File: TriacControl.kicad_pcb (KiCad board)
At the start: 2 copper layers, 100 x 53 mm, 55 parts, among them J1 AC LINE, J2 LOAD, J3 ZEROCROSS, J4 PWM, Q1 BT136-600, Q2 2N3906, U1 MOC3020M, U2 PC817, U3 PC817

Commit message: A few changes
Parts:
- added R27: 2k2, Resistor_THT:R_Axial_DIN0207_L6.3mm_D2.5mm_P7.62mm_Horizontal, F.Cu at (98.5, 94.1)
- Q2: value 2N3906 -> 2N2907
- R23, R24: value 100R -> 10R
- R25: value 10k -> 220R
- R26: value 22k -> 2k2
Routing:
- net Net-(D1-A): track 29.1 -> 38.0 mm
- net Net-(D2-A): track 16.8 -> 20.4 mm
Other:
- board text added: "MOC3021"
- board text removed: "MOC3081"
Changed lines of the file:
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@@
   )
   (footprint "Resistor_THT:R_Axial_DIN0207_L6.3mm_D2.5mm_P7.62mm_Horizontal" (layer "F.Cu")
+    (at 98.47 94.08 180)
+    (descr "Resistor, Axial_DIN0207 series, Axial, Horizontal, pin pitch=7.62mm, 0.25W = 1/4W, length*diameter=6.3*2.5mm^2, http://cdn-reichelt.de/documents/datenblatt/B400/1_4W%23YAG.pdf")
+    (tags "Resistor Axial_DIN0207 series Axial Horizontal pin pitch 7.62mm 0.25W = 1/4W length 6.3mm diameter 2.5mm")
+    (property "Sheetfile" "TriacControl.kicad_sch")
+    (property "Sheetname" "")
+    (property "ki_description" "Resistor")
+    (property "ki_keywords" "R res resistor")
+    (attr through_hole)
+    (fp_text reference "R27" (at 3.74 0.06) (layer "F.SilkS")
+        (effects (font (size 1 1) (thickness 0.15)))
+    )
+    (fp_text value "2k2" (at 3.81 2.37) (layer "F.Fab")
+        (effects (font (size 1 1) (thickness 0.15)))
+    )
+    (fp_text user "${REFERENCE}" (at 3.81 0) (layer "F.Fab")
+        (effects (font (size 1 1) (thickness 0.15)))
+    )
+    (fp_line (start 0.54 -1.37) (end 7.08 -1.37)
+      (stroke (width 0.12) (type solid)) (layer "F.SilkS"))
+    (fp_line (start 0.54 -1.04) (end 0.54 -1.37)
+      (stroke (width 0.12) (type solid)) (layer "F.SilkS"))
+    (fp_line (start 0.54 1.04) (end 0.54 1.37)
+      (stroke (width 0.12) (type solid)) (layer "F.SilkS"))
+    (fp_line (start 0.54 1.37) (end 7.08 1.37)
+      (stroke (width 0.12) (type solid)) (layer "F.SilkS"))
+    (fp_line (start 7.08 -1.37) (end 7.08 -1.04)
+      (stroke (width 0.12) (type solid)) (layer "F.SilkS"))
+    (fp_line (start 7.08 1.37) (end 7.08 1.04)
+      (stroke (width 0.12) (type solid)) (layer "F.SilkS"))
+    (fp_line (start -1.05 -1.5) (end -1.05 1.5)
+      (stroke (width 0.05) (type solid)) (layer "F.CrtYd"))
+    (fp_line (start -1.05 1.5) (end 8.67 1.5)
+      (stroke (width 0.05) (type solid)) (layer "F.CrtYd"))
+    (fp_line (start 8.67 -1.5) (end -1.05 -1.5)
+      (stroke (width 0.05) (type solid)) (layer "F.CrtYd"))
+    (fp_line (start 8.67 1.5) (end 8.67 -1.5)
+      (stroke (width 0.05) (type solid)) (layer "F.CrtYd"))
+    (fp_line (start 0 0) (end 0.66 0)
+      (stroke (width 0.1) (type solid)) (layer "F.Fab"))
+    (fp_line (start 0.66 -1.25) (end 0.66 1.25)
+      (stroke (width 0.1) (type solid)) (layer "F.Fab"))
+    (fp_line (start 0.66 1.25) (end 6.96 1.25)
+      (stroke (width 0.1) (type solid)) (layer "F.Fab"))
+    (fp_line (start 6.96 -1.25) (end 0.66 -1.25)
+      (stroke (width 0.1) (type solid)) (layer "F.Fab"))
+    (fp_line (start 6.96 1.25) (end 6.96 -1.25)
+      (stroke (width 0.1) (type solid)) (layer "F.Fab"))
+    (fp_line (start 7.62 0) (end 6.96 0)
+      (stroke (width 0.1) (type solid)) (layer "F.Fab"))
+    (pad "1" thru_hole circle (at 0 0 180) (size 1.6 1.6) (drill 0.8) (layers "*.Cu" "*.Mask")
+      (net 8 "Net-(D1-A)") (pintype "passive"))
+    (pad "2" thru_hole oval (at 7.62 0 180) (size 1.6 1.6) (drill 0.8) (layers "*.Cu" "*.Mask")
+      (net 9 "Net-(D2-A)") (pintype "passive"))
+    (model "${KICAD6_3DMODEL_DIR}/Resistor_THT.3dshapes/R_Axial_DIN0207_L6.3mm_D2.5mm_P7.62mm_Horizontal.wrl"
+      (offset (xyz 0 0 0))
+      (scale (xyz 1 1 1))
+      (rotate (xyz 0 0 0))
+    )
+  )
+  (footprint "Resistor_THT:R_Axial_DIN0207_L6.3mm_D2.5mm_P7.62mm_Horizontal" (layer "F.Cu")
     (at 115.85 62.2 -90)
     (descr "Resistor, Axial_DIN0207 series, Axial, Horizontal, pin pitch=7.62mm, 0.25W = 1/4W, length*diameter=6.3*2.5mm^2, http://cdn-reichelt.de/documents/datenblatt/B400/1_4W%23YAG.pdf")
@@
         (effects (font (size 1 1) (thickness 0.15)))
     )
-    (fp_text value "100R" (at 3.81 2.37 90) (layer "F.Fab")
+    (fp_text value "10R" (at 3.81 2.37 90) (layer "F.Fab")
         (effects (font (size 1 1) (thickness 0.15)))
     )
@@
         (effects (font (size 1 1) (thickness 0.15)))
     )
-    (fp_text value "100R" (at 3.81 2.37 90) (layer "F.Fab")
+    (fp_text value "10R" (at 3.81 2.37 90) (layer "F.Fab")
         (effects (font (size 1 1) (thickness 0.15)))
     )
@@
         (effects (font (size 1 1) (thickness 0.15)))
     )
-    (fp_text value "22k" (at 3.81 2.37) (layer "F.Fab")
+    (fp_text value "2k2" (at 3.81 2.37) (layer "F.Fab")
         (effects (font (size 1 1) (thickness 0.15)))
     )
@@
         (effects (font (size 1 1) (thickness 0.15)))
     )
-    (fp_text value "10k" (at 3.81 2.37) (layer "F.Fab")
+    (fp_text value "220R" (at 3.81 2.37) (layer "F.Fab")
         (effects (font (size 1 1) (thickness 0.15)))
     )
@@
         (effects (font (size 1 1) (thickness 0.15)))
     )
-    (fp_text value "2N3906" (at 2.54 2.79 90) (layer "F.Fab")
+    (fp_text value "2N2907" (at 2.54 2.79 90) (layer "F.Fab")
         (effects (font (size 1 1) (thickness 0.15)))
     )
@@
     (effects (font (size 1 1) (thickness 0.1)) (justify left bottom))
   )
-  (gr_text "PWM TRIAC CONTROLLER BY D. MARKS\nCC-BY-SA 4.0\nALL RISK IS ASSUMED BY USER\nHIGH VOLTAGE IS LETHAL!" (at 73.37 100.93) (layer "F.SilkS")
+  (gr_text "PWM TRIAC CONTROLLER BY D. MARKS\nCC-BY-SA 4.0\nALL RISK IS ASSUMED BY USER\nHIGH VOLTAGE IS LETHAL!" (at 61.28 101.56) (layer "F.SilkS")
     (effects (font (size 1 1) (thickness 0.1)) (justify left bottom))
   )
@@
     (effects (font (size 1 1) (thickness 0.1)) (justify left bottom))
   )
-  (gr_text "MOC3081" (at 105.24 70.58 90) (layer "F.SilkS")
+  (gr_text "MOC3021" (at 105.24 70.58 90) (layer "F.SilkS")
     (effects (font (size 1 1) (thickness 0.1)) (justify left bottom))
   )
@@
   (segment (start 92.25 79.8) (end 90.89 78.44) (width 2) (layer "F.Cu") (net 7))
   (segment (start 91.2 83.05) (end 91.2 80.85) (width 2) (layer "F.Cu") (net 7))
-  (segment (start 92.4 94.4) (end 94.7 92.1) (width 2) (layer "F.Cu") (net 8))
-  (segment (start 94.7 92.1) (end 94.7 90.67) (width 2) (layer "F.Cu") (net 8))
-  (segment (start 76.8 94.4) (end 92.4 94.4) (width 2) (layer "F.Cu") (net 8))
+  (segment (start 98.05 93.66) (end 98.47 94.08) (width 2) (layer "F.Cu") (net 8))
+  (segment (start 72.5 91.6) (end 74 91.6) (width 2) (layer "F.Cu") (net 8))
+  (segment (start 92.82 97.99) (end 94.7 96.11) (width 2) (layer "F.Cu") (net 8))
+  (segment (start 94.7 96.11) (end 94.7 90.67) (width 2) (layer "F.Cu") (net 8))
   (segment (start 98.01 90.7) (end 98.05 90.7) (width 2) (layer "F.Cu") (net 8))
   (segment (start 97.98 90.67) (end 98.01 90.7) (width 2) (layer "F.Cu") (net 8))
-  (segment (start 74 91.6) (end 76.8 94.4) (width 2) (layer "F.Cu") (net 8))
+  (segment (start 80.39 97.99) (end 92.82 97.99) (width 2) (layer "F.Cu") (net 8))
+  (segment (start 74 91.6) (end 80.39 97.99) (width 2) (layer "F.Cu") (net 8))
   (segment (start 94.7 90.67) (end 97.98 90.67) (width 2) (layer "F.Cu") (net 8))
-  (segment (start 72.5 91.6) (end 74 91.6) (width 2) (layer "F.Cu") (net 8))
+  (segment (start 98.05 90.7) (end 98.05 93.66) (width 2) (layer "F.Cu") (net 8))
   (segment (start 86.7 91.65) (end 79.34 91.65) (width 2) (layer "F.Cu") (net 9))
+  (segment (start 91.2 90.67) (end 91.2 93.73) (width 2) (layer "F.Cu") (net 9))
+  (segment (start 91.2 93.73) (end 90.85 94.08) (width 2) (layer "F.Cu") (net 9))
   (segment (start 90.97 90.9) (end 88.05 90.9) (width 2) (layer "F.Cu") (net 9))
   (segment (start 91.2 90.67) (end 90.97 90.9) (width 2) (layer "F.Cu") (net 9))

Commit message: Changed values, moved parts
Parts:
- C2: value 100 uF -> 47 uF
- C3: value 47 uF -> 22 uF
- C4: value 22 uF -> 10 uF
- R17, R18: value 1k -> 3k3
- R19: value 1k -> 820R
- R20: value 1k -> 330R
- moved Q1 5.50 mm to (75.8, 59.0)
- moved R15 4.07 mm to (87.8, 62.8)
- moved R13 4.02 mm to (94.3, 62.7)
- moved R14 3.93 mm to (91.0, 62.8)
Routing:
- net Net-(J1-Pin_1): track 78.5 -> 90.4 mm
- net Net-(J2-Pin_1): track 72.3 -> 64.3 mm
- net Net-(Q1-G): track 35.4 -> 31.5 mm
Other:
- board text added: "DANGER DO NOT TOUCH BOARD OR COMPONENTS WHEN OPERATING!"
- board text removed: "DANGER DO NOT TOUCH THIS SIDE WHEN OPERATING!"

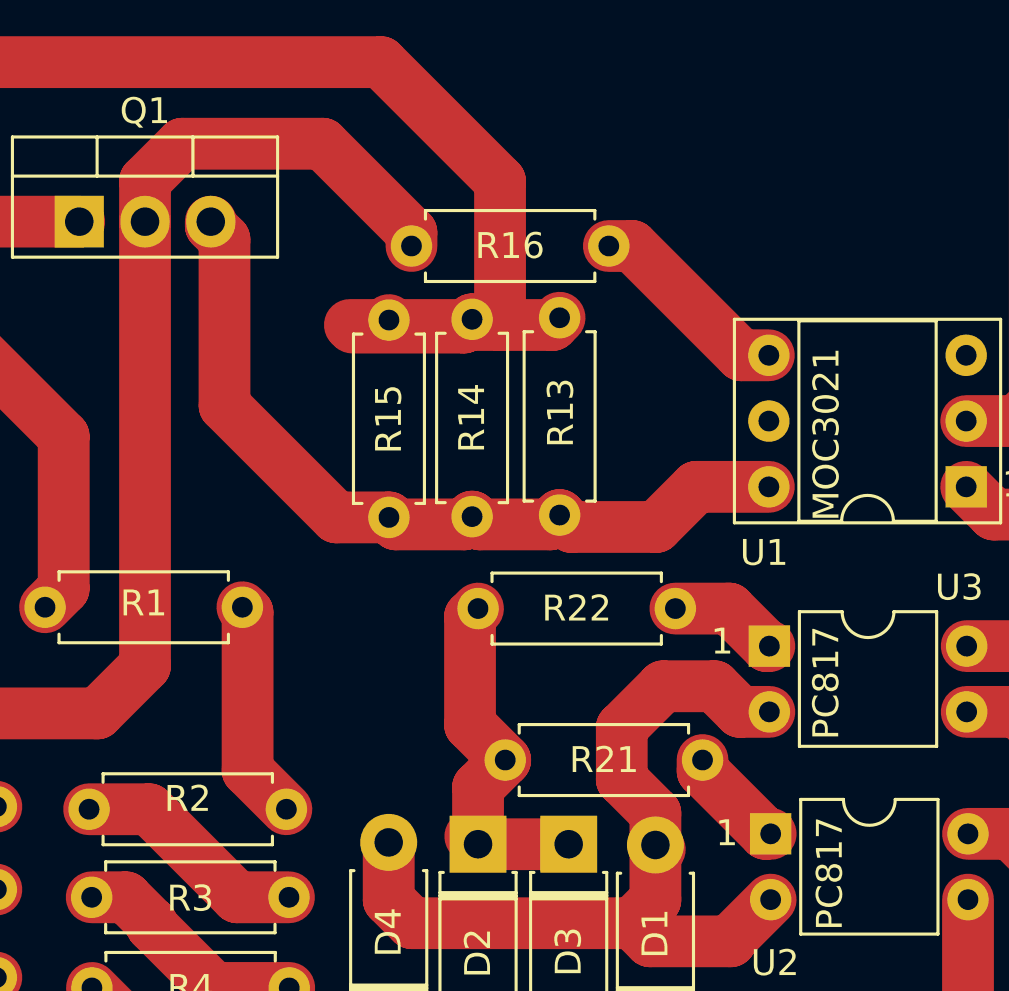
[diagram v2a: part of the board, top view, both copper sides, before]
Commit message: Fixed names and traces
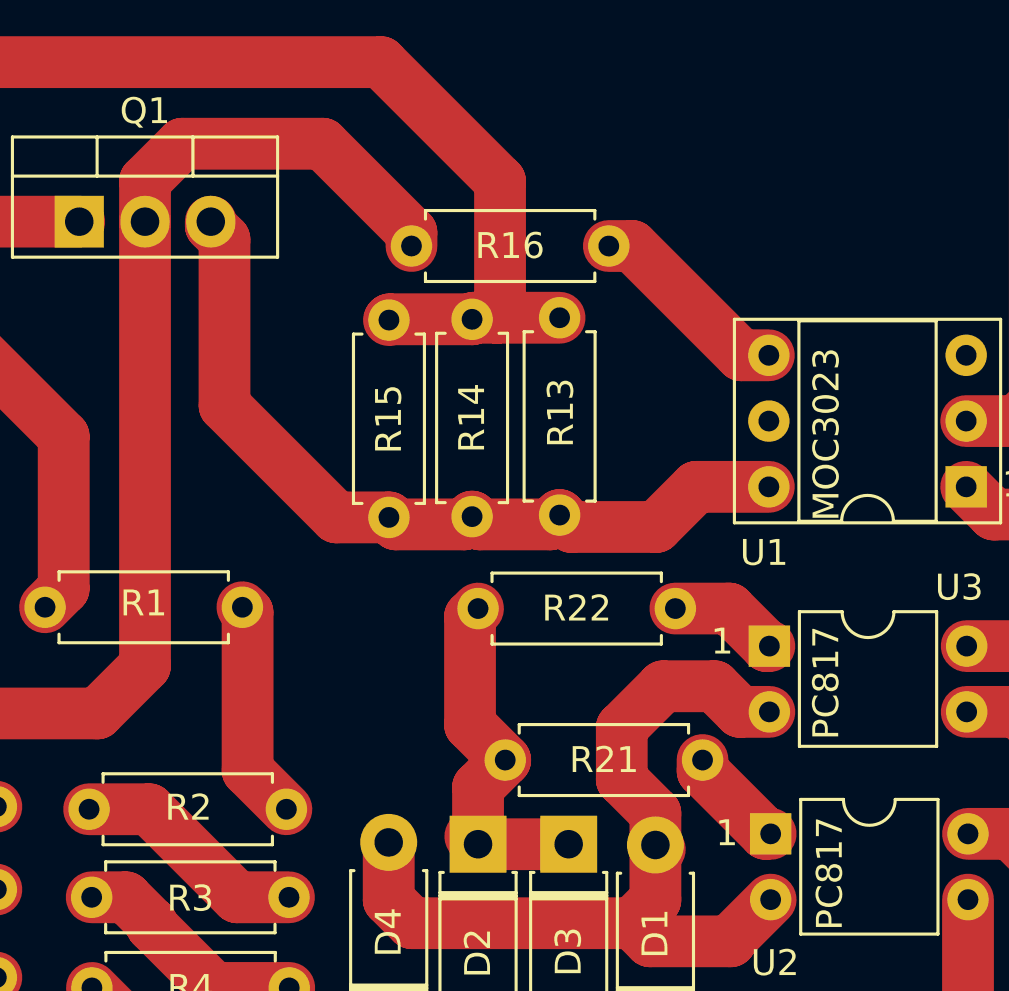
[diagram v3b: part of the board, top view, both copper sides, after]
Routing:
- net Net-(J1-Pin_1): track 90.4 -> 80.4 mm
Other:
- board text added: "MOC3023"
- board text removed: "MOC3021"
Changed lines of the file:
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@@
     (property "ki_keywords" "R res resistor")
     (attr through_hole)
-    (fp_text reference "R2" (at 3.81 -0.4) (layer "F.SilkS")
+    (fp_text reference "R2" (at 3.84 -0.06) (layer "F.SilkS")
         (effects (font (size 1 1) (thickness 0.15)))
     )
@@
     (effects (font (size 1 1) (thickness 0.1)) (justify left bottom))
   )
-  (gr_text "MOC3021" (at 105.24 70.58 90) (layer "F.SilkS")
+  (gr_text "MOC3023" (at 105.24 70.58 90) (layer "F.SilkS")
     (effects (font (size 1 1) (thickness 0.1)) (justify left bottom))
   )
@@
   )
   (segment (start 69.1 62.9) (end 69.1 59.5) (width 2) (layer "F.Cu") (net 1))
+  (segment (start 92.05 57.45) (end 92.05 62.6) (width 2) (layer "F.Cu") (net 1))
   (segment (start 75.8 59.01) (end 69.59 59.01) (width 2) (layer "F.Cu") (net 1))
   (segment (start 69.59 59.01) (end 69.1 59.5) (width 2) (layer "F.Cu") (net 1))
+  (segment (start 94.35 62.72) (end 91.93 62.72) (width 2) (layer "F.Cu") (net 1))
   (segment (start 75.2 67.3) (end 75.2 73.18) (width 2) (layer "F.Cu") (net 1))
+  (segment (start 92.05 62.6) (end 91.93 62.72) (width 2) (layer "F.Cu") (net 1))
   (segment (start 68.4 58.8) (end 68.4 54.4) (width 2) (layer "F.Cu") (net 1))
   (segment (start 87.45 52.85) (end 92.05 57.45) (width 2) (layer "F.Cu") (net 1))
@@
   (segment (start 75.2 73.18) (end 74.48 73.9) (width 2) (layer "F.Cu") (net 1))
   (segment (start 68.4 54.4) (end 69.95 52.85) (width 2) (layer "F.Cu") (net 1))
-  (segment (start 94.35 62.72) (end 94.07 63) (width 2) (layer "F.Cu") (net 1))
-  (segment (start 90.7 63.05) (end 90.97 62.78) (width 2) (layer "F.Cu") (net 1))
-  (segment (start 92.05 62.98) (end 92.03 63) (width 2) (layer "F.Cu") (net 1))
-  (segment (start 94.07 63) (end 92.03 63) (width 2) (layer "F.Cu") (net 1))
-  (segment (start 90.65 63.1) (end 90.97 62.78) (width 2) (layer "F.Cu") (net 1))
+  (segment (start 87.79 62.78) (end 87.76 62.81) (width 2) (layer "F.Cu") (net 1))
+  (segment (start 91.03 62.72) (end 90.97 62.78) (width 2) (layer "F.Cu") (net 1))
   (segment (start 69.95 52.85) (end 87.45 52.85) (width 2) (layer "F.Cu") (net 1))
+  (segment (start 91.93 62.72) (end 91.03 62.72) (width 2) (layer "F.Cu") (net 1))
   (segment (start 69.1 62.9) (end 70.8 62.9) (width 2) (layer "F.Cu") (net 1))
-  (segment (start 87.76 62.81) (end 88 63.05) (width 2) (layer "F.Cu") (net 1))
-  (segment (start 92.03 63) (end 86.25 63) (width 2) (layer "F.Cu") (net 1))
   (segment (start 70.8 62.9) (end 75.2 67.3) (width 2) (layer "F.Cu") (net 1))
-  (segment (start 88 63.05) (end 90.7 63.05) (width 2) (layer "F.Cu") (net 1))
   (segment (start 69.1 59.5) (end 68.4 58.8) (width 2) (layer "F.Cu") (net 1))
-  (segment (start 92.05 57.45) (end 92.05 62.98) (width 2) (layer "F.Cu") (net 1))
-  (segment (start 86.35 63.1) (end 90.65 63.1) (width 2) (layer "F.Cu") (net 1))
   (segment (start 61 58.8) (end 57.95 61.85) (width 2) (layer "F.Cu") (net 1))
+  (segment (start 90.97 62.78) (end 87.79 62.78) (width 2) (layer "F.Cu") (net 1))
   (segment (start 64.1 67.4) (end 64 67.5) (width 2) (layer "F.Cu") (net 2))
   (segment (start 64 74) (end 64 70.8) (width 2) (layer "F.Cu") (net 2))

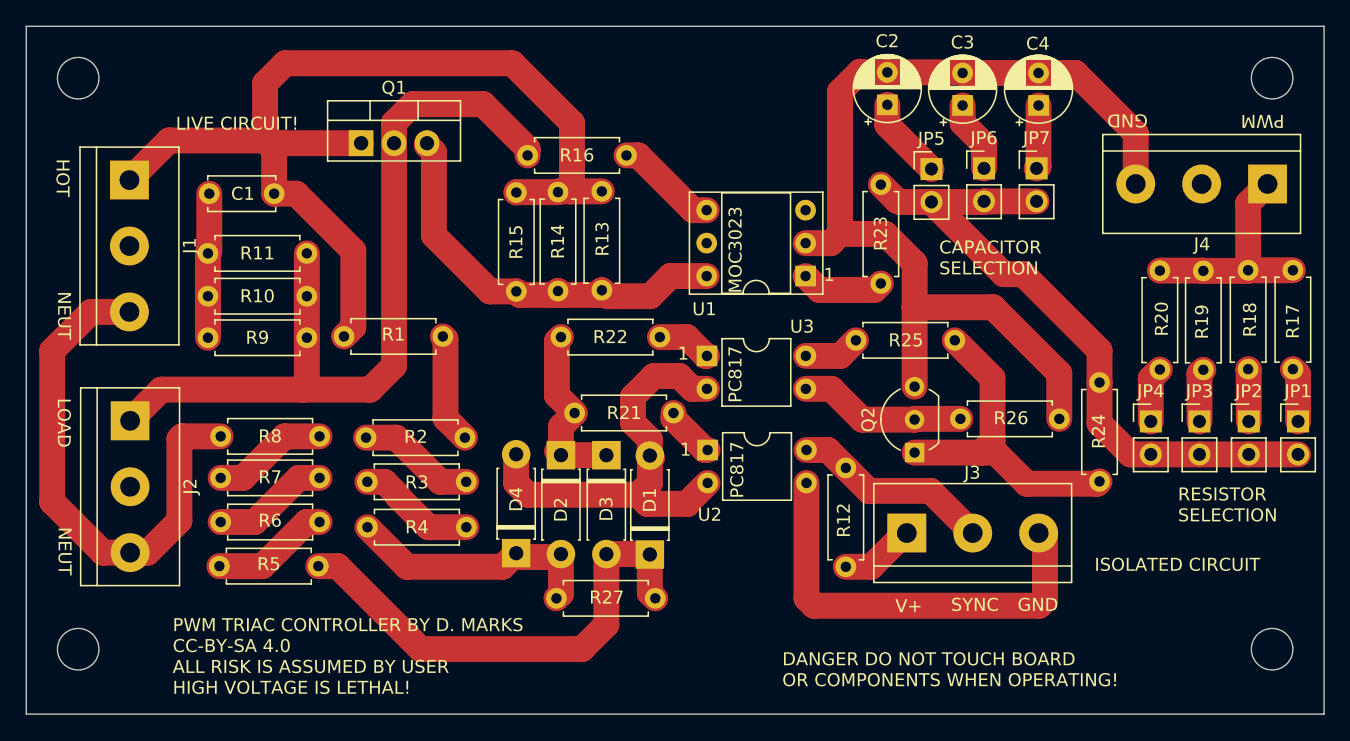
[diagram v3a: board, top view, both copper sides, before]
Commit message: Changed connection to snubber, resistor size, etc.
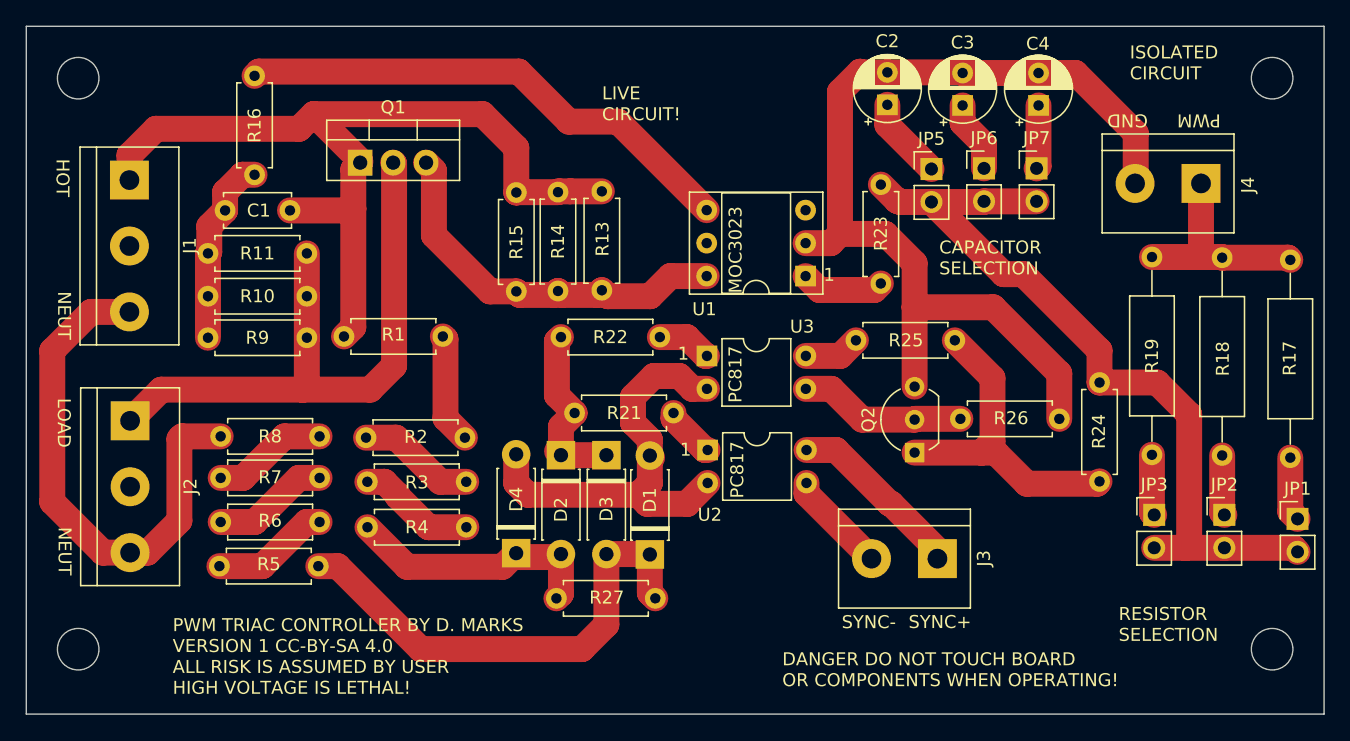
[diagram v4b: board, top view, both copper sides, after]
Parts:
- removed JP4: Pinhead, Connector_PinHeader_2.54mm:PinHeader_1x02_P2.54mm_Vertical
- removed R12: 1k, Resistor_THT:R_Axial_DIN0207_L6.3mm_D2.5mm_P7.62mm_Horizontal
- removed R20: 330R, Resistor_THT:R_Axial_DIN0207_L6.3mm_D2.5mm_P7.62mm_Horizontal
- J3, J4: footprint TerminalBlock:TerminalBlock_bornier-3_P5.08mm -> TerminalBlock:TerminalBlock_bornier-2_P5.08mm
- R17, R18, R19: footprint Resistor_THT:R_Axial_DIN0207_L6.3mm_D2.5mm_P7.62mm_Horizontal -> Resistor_THT:R_Axial_DIN0309_L9.0mm_D3.2mm_P15.24mm_Horizontal
- U1: value MOC3020M -> MOC3023
- moved R16 29.3 mm to (67.6, 53.8), turned to -90 degrees
- moved JP3 8.00 mm to (136.9, 87.7)
- moved JP1 7.51 mm to (148.0, 88.0)
- moved JP2 7.44 mm to (142.3, 87.7)
- moved J4 5.13 mm to (140.5, 62.1)
- moved R19 4.10 mm to (136.7, 67.8)
- moved J3 3.07 mm to (120.2, 91.0), turned to 180 degrees
- moved R18 2.22 mm to (142.2, 67.8)
- moved C1 1.78 mm to (70.3, 64.2)
- moved Q1 1.50 mm to (75.7, 60.5)
- moved R17 0.82 mm to (147.4, 68.0)
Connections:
- J3 pad 2: Net-(J3-Pin_2) -> GND
- J4 pad 2: unconnected-(J4-Pin_2-Pad2) -> GND2
- R16 pad 2: Net-(J2-Pin_1) -> Net-(C1-Pad2)
- U2 pad 4: Net-(J3-Pin_2) -> Net-(J3-Pin_1)
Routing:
- net Net-(R16-Pad1): track 7.93 -> 39.4 mm
- net GND: track 33.0 -> 7.91 mm
- net Net-(J2-Pin_1): track 64.3 -> 48.4 mm
- net Net-(J3-Pin_2): track 15.5 -> 0.00 mm
- net Net-(J1-Pin_1): track 80.4 -> 68.2 mm
- net Net-(JP1-B): track 52.2 -> 62.2 mm
- net Net-(J3-Pin_1): track 5.78 -> 13.9 mm
- net Net-(JP4-A): track 4.29 -> 0.00 mm
- net Net-(C1-Pad2): track 11.1 -> 14.6 mm
- net Net-(Q1-G): track 31.5 -> 30.0 mm
- net Net-(J4-Pin_1): track 17.6 -> 16.5 mm
- net Net-(JP1-A): track 4.20 -> 4.95 mm
- net Net-(JP2-A): track 4.05 -> 4.65 mm
- net Net-(JP3-A): track 4.10 -> 4.70 mm
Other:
- board text added: "PWM TRIAC CONTROLLER BY D. MARKS VERSION 1 CC-BY-SA 4.0 ALL RISK IS ASSUMED BY USER HIGH VOLTAGE IS LETHAL!"
- board text added: "SYNC+"
- board text added: "SYNC-"
- board text removed: "PWM TRIAC CONTROLLER BY D. MARKS CC-BY-SA 4.0 ALL RISK IS ASSUMED BY USER HIGH VOLTAGE IS LETHAL!"
- board text removed: "SYNC"
- board text removed: "V+"
